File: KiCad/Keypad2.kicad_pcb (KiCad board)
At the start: 2 copper layers, 13.2 x 29 mm, 18 parts, among them J1 Keypad, J2 Prog, U1 SP3485, U2 ESP32-PICO-MINI-02, U3 LMR16006+FB, U4 QR

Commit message: Tweak, getting ready to order
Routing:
- net O: track 21.5 -> 22.3 mm

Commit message: DRC tidy
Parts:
- moved U3 0.05 mm to (171.3, 110.5)
- moved R5 0.05 mm to (173.4, 107.6)
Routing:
- net GND: track 63.4 -> 30.6 mm
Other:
- rule pad_to_mask_clearance: 0 -> 0.125

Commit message: Tweak DRC
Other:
- rule pad_to_mask_clearance: 0.125 -> 0.01
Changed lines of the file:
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@@
       (dielectric_constraints no)
     )
-    (pad_to_mask_clearance 0.125)
+    (pad_to_mask_clearance 0.01)
     (pad_to_paste_clearance_ratio -0.02)
     (pcbplotparams

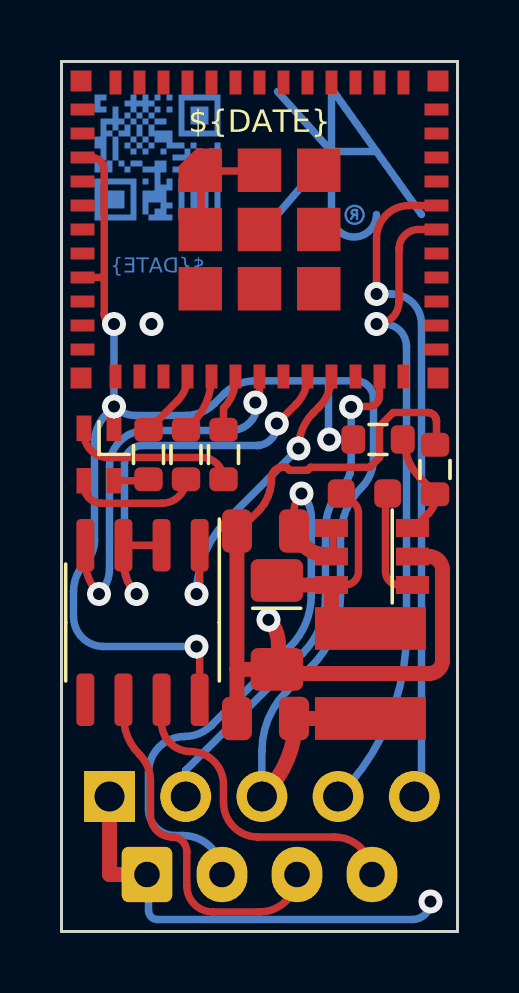
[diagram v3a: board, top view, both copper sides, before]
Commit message: Resistor fixes
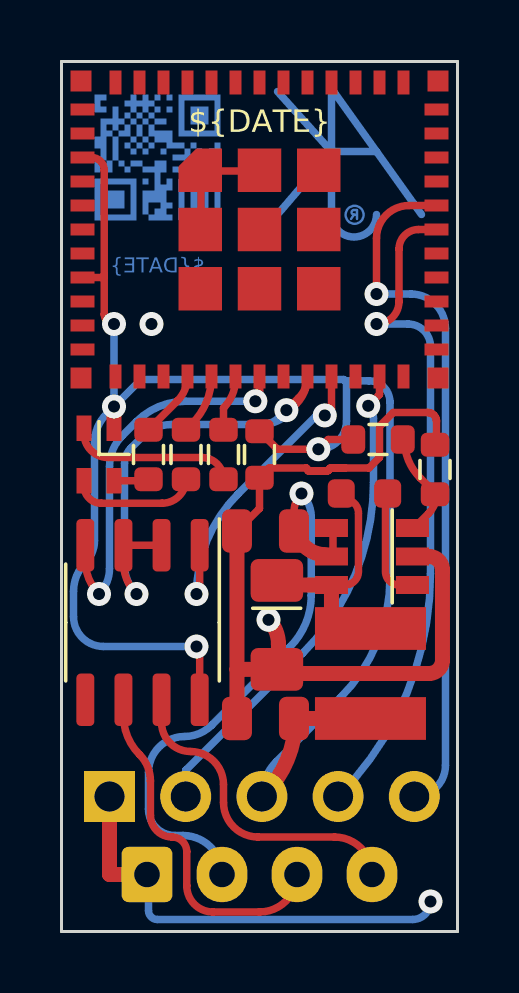
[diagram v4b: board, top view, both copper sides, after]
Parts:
- added C4: 100nF, RevK:C_0603, F.Cu at (167.6, 107.1)
- R4: value 10M 1% or 0R -> 100k 1% or 0R
- R5: value 3M 1% or NF -> 30k 1% or NF
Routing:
- net +3V3: track 53.7 -> 58.0 mm
- net DE: track 15.3 -> 17.0 mm
- net GND: track 30.6 -> 32.2 mm
- net O: track 22.3 -> 23.5 mm
- net I: track 21.5 -> 22.5 mm
- net TX: track 13.1 -> 13.8 mm

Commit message: C/R on EN
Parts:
- added C1: 10nF, RevK:C_0603, F.Cu at (162.4, 116.7)
- added R1: 10K, RevK:R_0603, F.Cu at (164.9, 116.7)
- moved U1 0.15 mm to (163.7, 112.5)
- renumbered C1 to C2, C2 to C3, C3 to C4, C4 to C5, R1 to R2, R2 to R3, R3 to R4, R4 to R5, R5 to R6
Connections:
- U2 pad 8: +3V3 -> Net-(C1-Pad2)
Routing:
- net Net-(C1-Pad2): track 0.00 -> 20.1 mm, vias 0 -> 2
- net GND: track 32.2 -> 52.0 mm, vias 3 -> 4
- net DE: track 17.0 -> 12.8 mm
- net Net-(J1-Pad4): track 10.7 -> 14.8 mm
- net +12V: track 19.0 -> 15.6 mm
- net Net-(J1-Pad3): track 11.9 -> 14.7 mm, vias 0 -> 1
- net TX: track 13.8 -> 11.5 mm
- net GPIO0: track 16.4 -> 17.5 mm
- net +3V3: track 58.0 -> 57.0 mm

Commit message: Library update
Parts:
- moved R6 0.20 mm to (173.4, 107.4)
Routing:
- net GND: track 52.0 -> 48.7 mm, vias 4 -> 3
- net Net-(J1-Pad3): track 14.7 -> 15.8 mm

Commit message: Schematic cleanup
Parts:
- C2: footprint RevK:Hidden -> RevK:C_0603_
- C3, C4: footprint RevK:Hidden -> RevK:C_0805_
- D2: footprint RevK:Hidden -> RevK:D_1206_
- J2: value Prog -> Shelly; footprint Connector_PinHeader_2.54mm:PinHeader_1x05_P2.54mm_Vertical -> RevK:Shelly
- L1: footprint RevK:Hidden -> RevK:L_4x4_
- U3: footprint RevK:RegulatorBlockFB -> RevK:SOT-23-Thin-6-Reg
- moved J2 5.10 mm to (167.7, 118.5), turned to 180 degrees
- moved U3 0.05 mm to (171.4, 110.5)

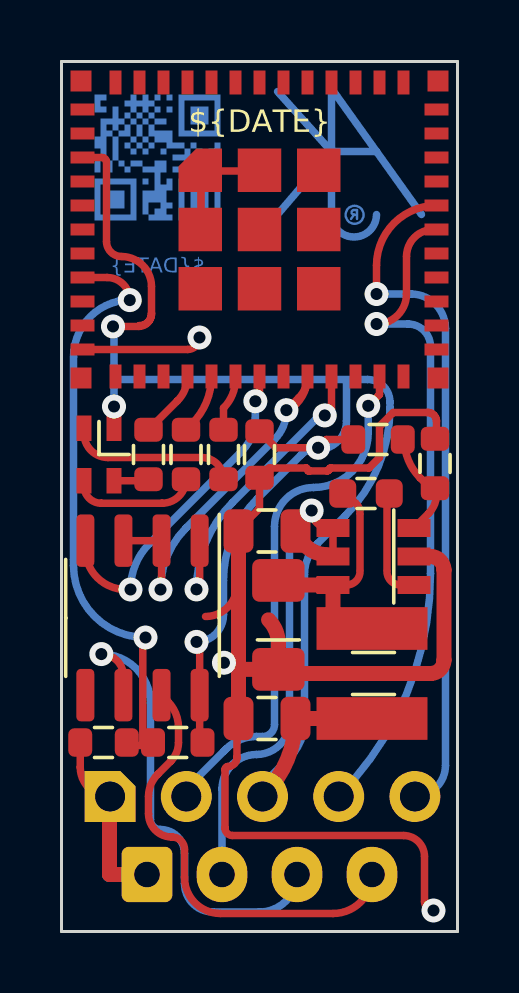
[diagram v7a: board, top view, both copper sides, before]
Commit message: Backwards diode
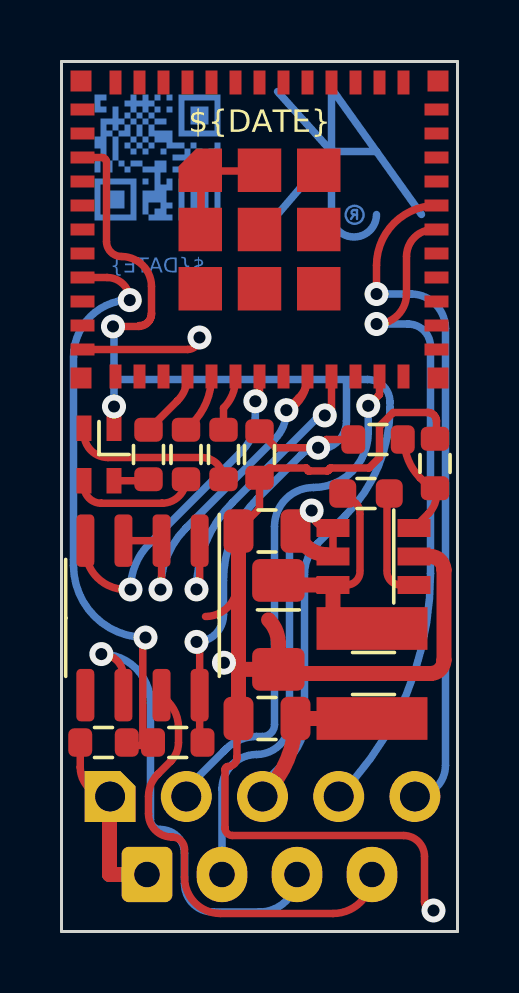
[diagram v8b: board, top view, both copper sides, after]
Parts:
- turned D2 to -90 degrees
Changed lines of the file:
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@@
   )
   (footprint "RevK:D_1206_" (layer "F.Cu")
-    (at 168.23 112.78 90)
+    (at 168.23 112.78 -90)
     (property "Manufacturer" "Bourns")
     (property "Note" "")
@@
       (effects (font (size 0.5 0.5) (thickness 0.08)))
     )
-    (fp_text user "D" (at -0.8 0 90 unlocked) (layer "F.Fab")
+    (fp_text user "D" (at -0.8 0 -90 unlocked) (layer "F.Fab")
       (effects (font (size 0.5 0.5) (thickness 0.08)))
     )
